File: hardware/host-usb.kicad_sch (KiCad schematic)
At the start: 24 parts, among them IC10 DSC6101CI2A-024.0000, IC8 I2C-EEPROM, IC9 CY7C68013A-56PVXC

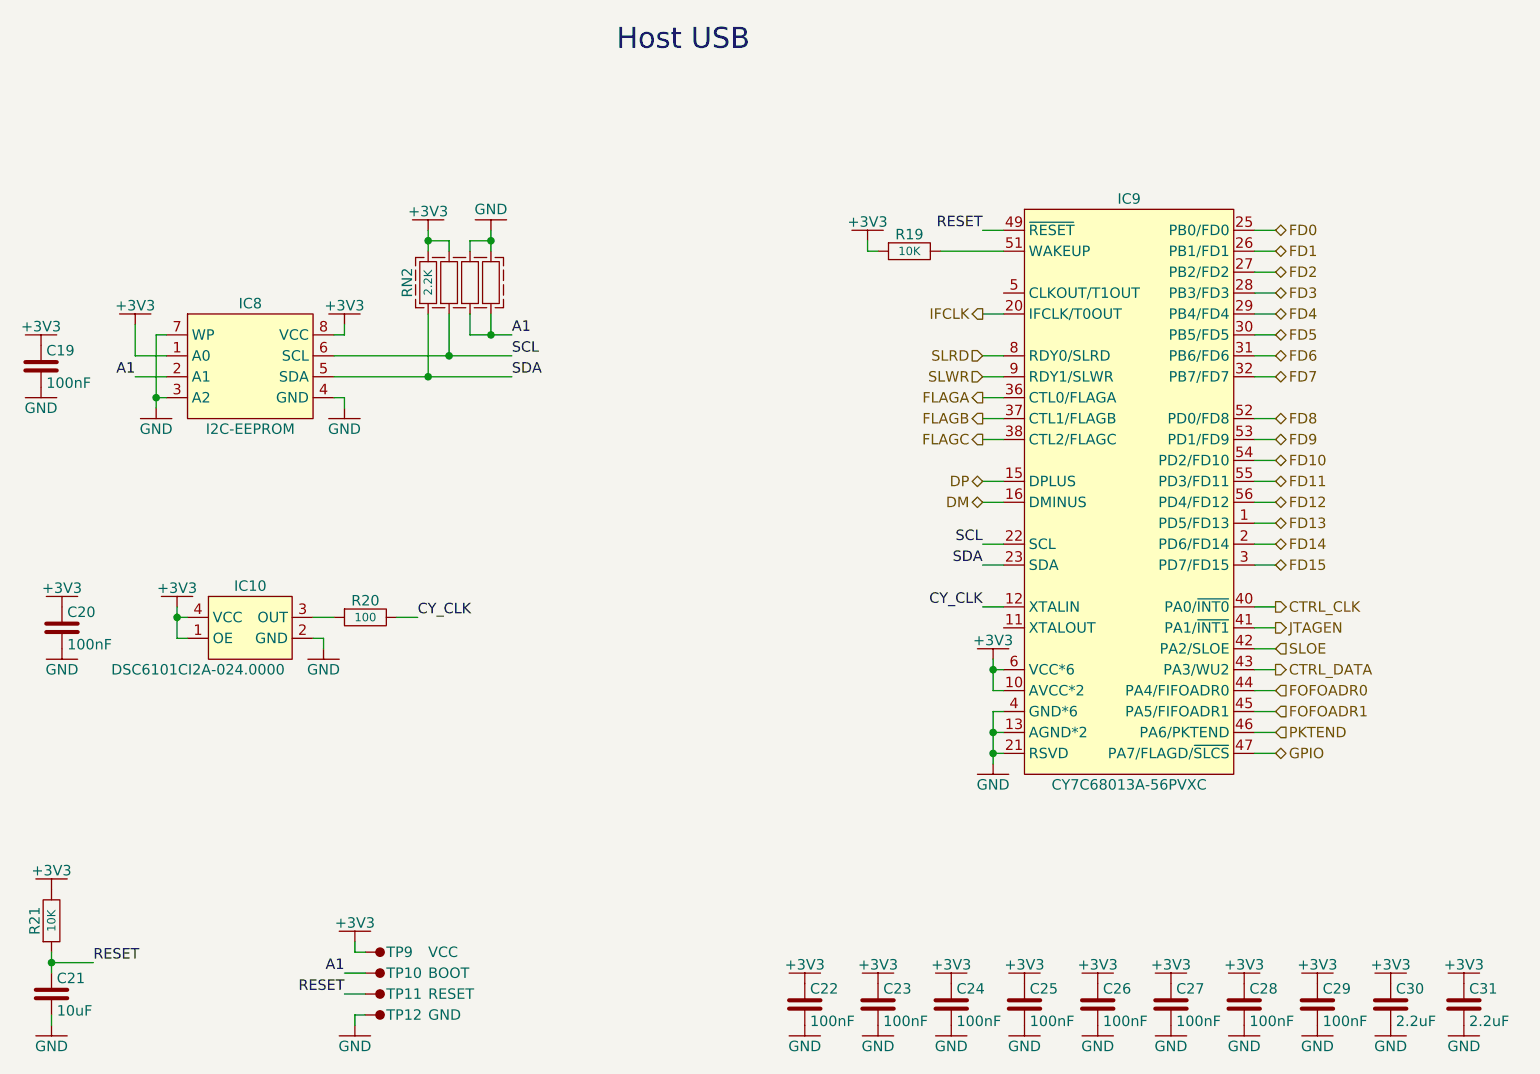
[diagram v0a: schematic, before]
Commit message: Use a single large sheet for the schematic
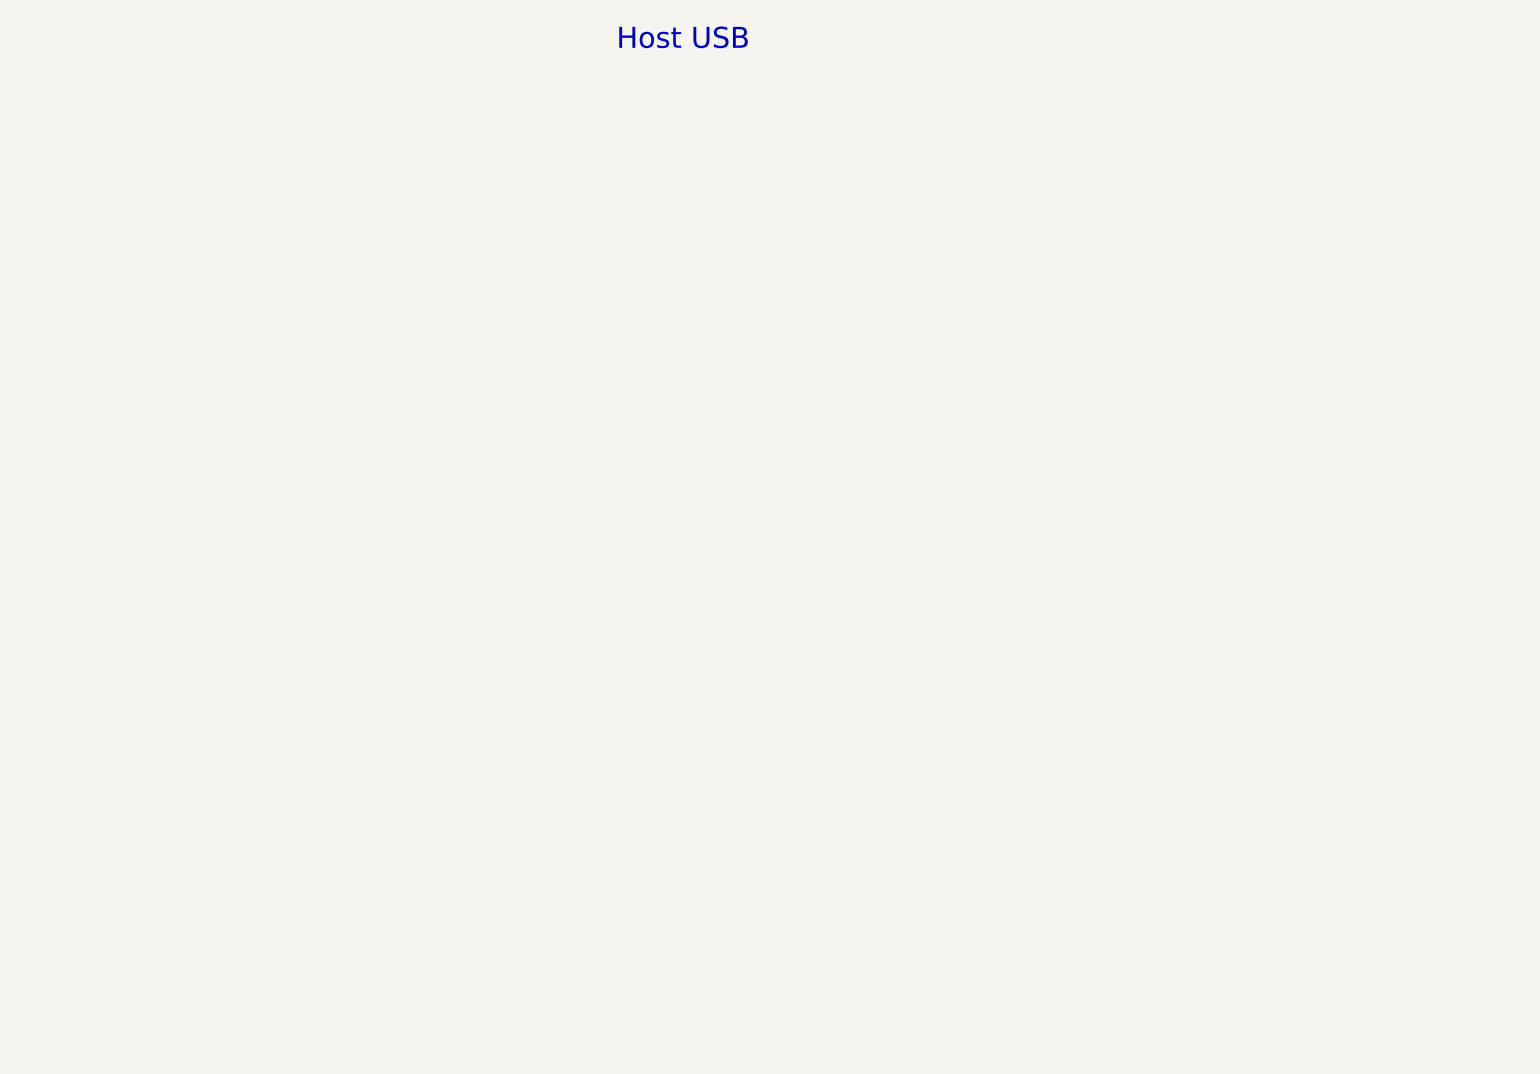
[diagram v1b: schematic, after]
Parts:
- removed C19, C20, C22, C23, C24, C25, C26, C27, C28, C29: 100nF, ataradov_smd:0603, symbol ataradov_rlc:C
- removed C21: 10uF, ataradov_smd:0603, symbol ataradov_rlc:C
- removed C30, C31: 2.2uF, ataradov_smd:0603, symbol ataradov_rlc:C
- removed IC10: DSC6101CI2A-024.0000, ataradov_ic:CDFN-4-3.2x2.5mm, symbol ataradov_crystal:DSC61XX-MHz
- removed IC8: I2C-EEPROM, ataradov_ic:SO-8, symbol ataradov_ic:I2C-EEPROM
- removed IC9: CY7C68013A-56PVXC, ataradov_ic:SSOP-56-0.635mm, symbol ataradov_mcu:CY7C68013A-56PVXC
- removed R19, R21: 10K, ataradov_smd:0603, symbol ataradov_rlc:R
- removed R20: 100, ataradov_smd:0603, symbol ataradov_rlc:R
- removed RN2: 2.2K, ataradov_smd:0603x4, symbol ataradov_rlc:RN-4
- removed TP10: BOOT, ataradov_misc:TestPoint-1.27mm, symbol ataradov_misc:TestPoint
- removed TP11: RESET, ataradov_misc:TestPoint-1.27mm, symbol ataradov_misc:TestPoint
- removed TP12: GND, ataradov_misc:TestPoint-1.27mm, symbol ataradov_misc:TestPoint
- removed TP9: VCC, ataradov_misc:TestPoint-1.27mm, symbol ataradov_misc:TestPoint
